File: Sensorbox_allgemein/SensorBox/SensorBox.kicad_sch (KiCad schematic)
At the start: 29 parts, among them J1 SD_Card, Q1 NPN, U2 PS1-O3-100, U3 Beetle ESP32-C6, U5 HPP845E131R5, U6 TPS629211QDRLRQ1

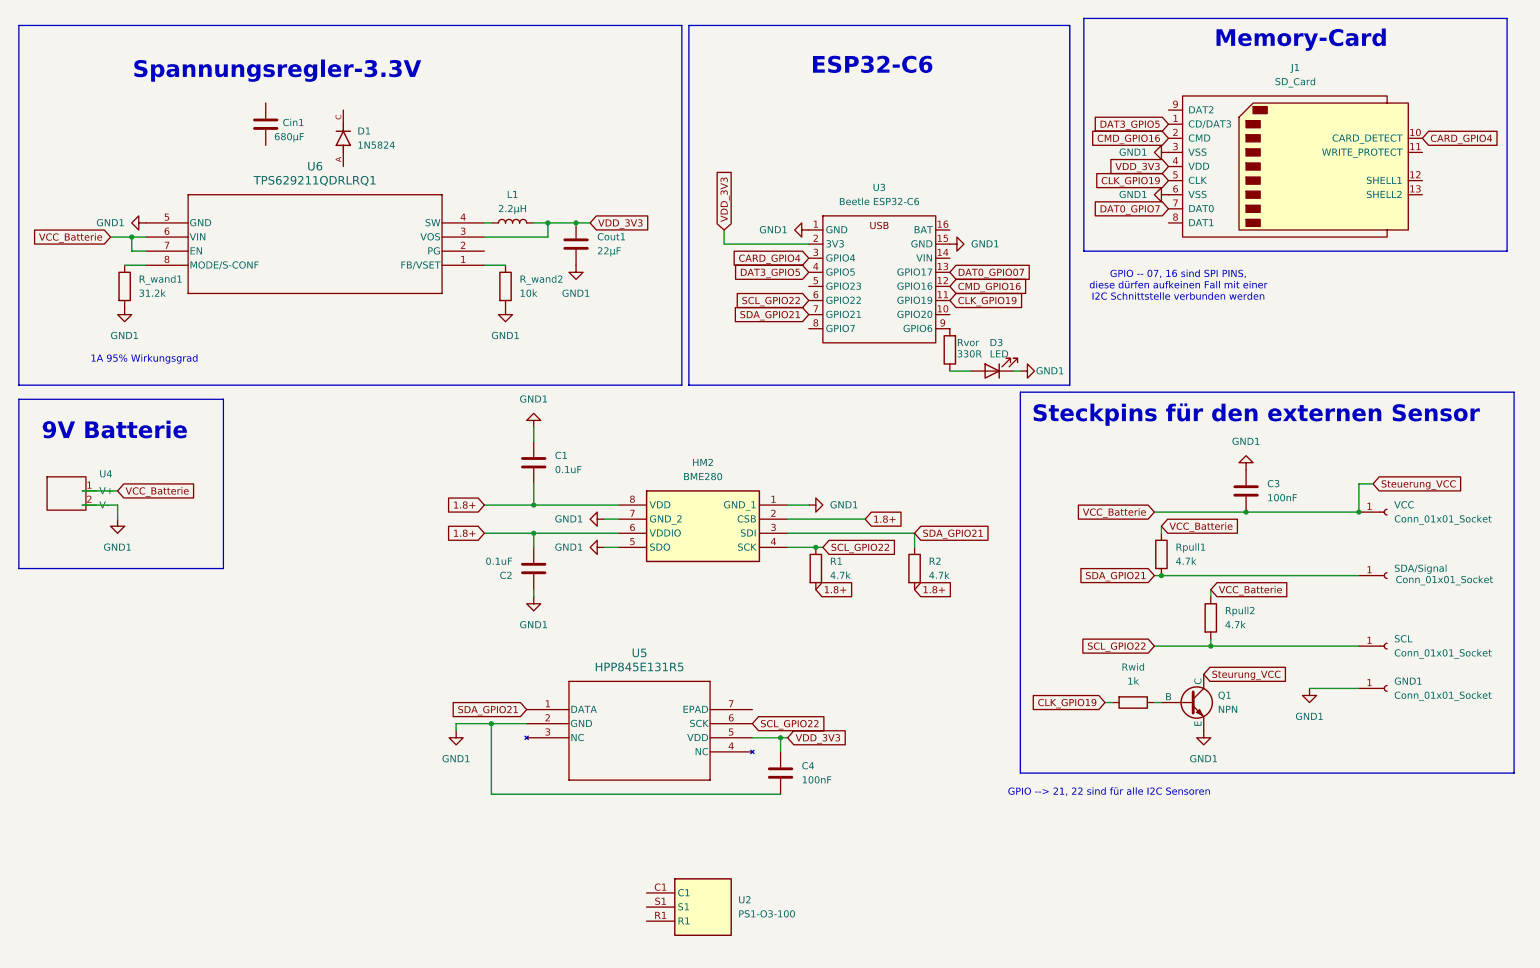
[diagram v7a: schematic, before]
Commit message: Update SensorBox.kicad_sch
pin Belegungen geändert, bzw. angepasst zum Messaufbau. Speziell GPIO20, 19
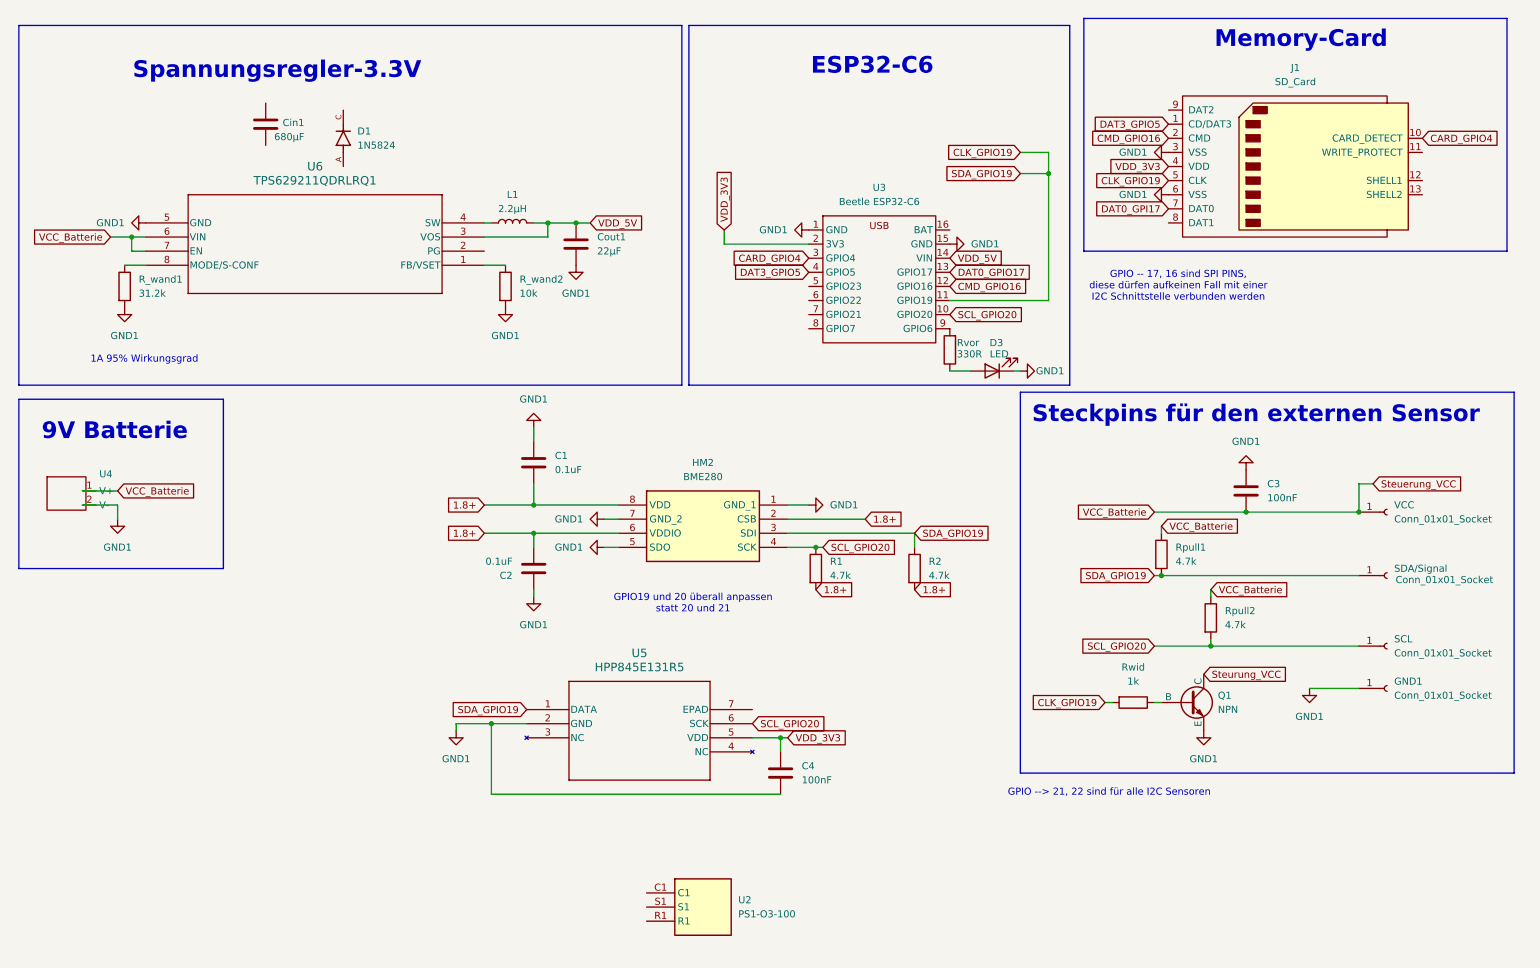
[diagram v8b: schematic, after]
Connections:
- net CLK_GPIO19: now also HM2.3 (SDI), R2.1, Rpull1.2, SDA/Signal.1 (Pin_1), U5.1 (DATA)
- net VDD_3V3: no longer Cout1.1, L1.2, U6.3 (VOS)
- net SCL_GPIO20: now reaches U3.10 (GPIO20)
- net SCL_GPIO20: now also HM2.4 (SCK), R1.1, Rpull2.2, SCL.1 (Pin_1), U5.6 (SCK)
- net VDD_5V: now reaches U3.14 (VIN)
- net VDD_5V: now also Cout1.1, L1.2, U6.3 (VOS)
- net DAT0_GPIO07 renamed DAT0_GPIO17
- net DAT0_GPIO7 renamed DAT0_GPI17
- removed net SCL_GPIO22: HM2.4 (SCK), R1.1, Rpull2.2, SCL.1 (Pin_1), U3.6 (GPIO22), U5.6 (SCK)
- removed net SDA_GPIO21: HM2.3 (SDI), R2.1, Rpull1.2, SDA/Signal.1 (Pin_1), U3.7 (GPIO21), U5.1 (DATA)
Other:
- note added: "GPIO -- 17, 16 sind SPI PINS, diese dürfen aufkeinen Fall mit einer I2C Schnittstelle verbunden werden"
- note added: "GPIO19 und 20 überall anpassen statt 20 und 21"
- note removed: "GPIO -- 07, 16 sind SPI PINS, diese dürfen aufkeinen Fall mit einer I2C Schnittstelle verbunden werden"
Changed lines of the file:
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@@
+	)
+	(junction
+		(at 199.39 41.91)
+		(diameter 0)
+		(color 0 0 0 0)
 	)
 	(junction
@@
 	(wire
 		(pts
+			(xy 194.31 38.1) (xy 199.39 38.1)
+		)
+		(stroke
+			(width 0)
+			(type default)
+		)
+	)
+	(wire
+		(pts
 			(xy 99.06 153.67) (xy 99.06 140.97)
 		)
@@
 	(wire
 		(pts
+			(xy 199.39 64.77) (xy 181.61 64.77)
+		)
+		(stroke
+			(width 0)
+			(type default)
+		)
+	)
+	(wire
+		(pts
 			(xy 31.75 104.14) (xy 31.75 101.6)
 		)
@@
 	(wire
 		(pts
+			(xy 199.39 38.1) (xy 199.39 41.91)
+		)
+		(stroke
+			(width 0)
+			(type default)
+		)
+	)
+	(wire
+		(pts
 			(xy 101.6 58.42) (xy 97.79 58.42)
 		)
@@
 	(wire
 		(pts
+			(xy 194.31 41.91) (xy 199.39 41.91)
+		)
+		(stroke
+			(width 0)
+			(type default)
+		)
+	)
+	(wire
+		(pts
 			(xy 234.95 102.87) (xy 255.27 102.87)
 		)
@@
 		(pts
 			(xy 228.6 127) (xy 255.27 127)
+		)
+		(stroke
+			(width 0)
+			(type default)
+		)
+	)
+	(wire
+		(pts
+			(xy 199.39 41.91) (xy 199.39 64.77)
 		)
 		(stroke
@@
 		)
 	)
-	(text "GPIO -- 07, 16 sind SPI PINS, \ndiese dürfen aufkeinen Fall mit einer \nI2C Schnittstelle verbunden werden"
+	(text "GPIO19 und 20 überall anpassen\nstatt 20 und 21\n"
+		(exclude_from_sim no)
+		(at 135.382 119.38 0)
+		(effects
+			(font
+				(size 1.27 1.27)
+			)
+		)
+	)
+	(text "GPIO -- 17, 16 sind SPI PINS, \ndiese dürfen aufkeinen Fall mit einer \nI2C Schnittstelle verbunden werden"
 		(exclude_from_sim no)
 		(at 222.758 62.23 0)
@@
 		)
 	)
-	(global_label "SCL_GPIO22"
+	(global_label "SCL_GPIO20"
 		(shape input)
 		(at 146.05 140.97 0)
@@
 	(global_label "CLK_GPIO19"
 		(shape input)
-		(at 181.61 64.77 0)
-		(fields_autoplaced yes)
-		(effects
-			(font
-				(size 1.27 1.27)
-			)
-			(justify left)
-		)
-		(property "Intersheetrefs" "${INTERSHEET_REFS}"
-			(at 196.0252 64.77 0)
-			(effects
-				(font
-					(size 1.27 1.27)
-				)
-				(justify left)
-				(hide yes)
-			)
-		)
-	)
-	(global_label "SDA_GPIO21"
+		(at 194.31 38.1 180)
+		(fields_autoplaced yes)
+		(effects
+			(font
+				(size 1.27 1.27)
+			)
+			(justify right)
+		)
+		(property "Intersheetrefs" "${INTERSHEET_REFS}"
+			(at 179.8948 38.1 0)
+			(effects
+				(font
+					(size 1.27 1.27)
+				)
+				(justify right)
+				(hide yes)
+			)
+		)
+	)
+	(global_label "SDA_GPIO19"
 		(shape input)
 		(at 105.41 138.43 180)
@@
 		)
 	)
-	(global_label "SCL_GPIO22"
+	(global_label "SCL_GPIO20"
 		(shape input)
 		(at 158.75 109.22 0)
@@
 		)
 	)
-	(global_label "SDA_GPIO21"
+	(global_label "SDA_GPIO19"
 		(shape input)
 		(at 175.26 106.68 0)
@@
 		)
 	)
+	(global_label "SCL_GPIO20"
+		(shape input)
+		(at 181.61 67.31 0)
+		(fields_autoplaced yes)
+		(effects
+			(font
+				(size 1.27 1.27)
+			)
+			(justify left)
+		)
+		(property "Intersheetrefs" "${INTERSHEET_REFS}"
+			(at 195.9647 67.31 0)
+			(effects
+				(font
+					(size 1.27 1.27)
+				)
+				(justify left)
+				(hide yes)
+			)
+		)
+	)
 	(global_label "1.8+"
 		(shape input)
@@
 		)
 	)
+	(global_label "VDD_5V"
+		(shape input)
+		(at 181.61 57.15 0)
+		(fields_autoplaced yes)
+		(effects
+			(font
+				(size 1.27 1.27)
+			)
+			(justify left)
+		)
+		(property "Intersheetrefs" "${INTERSHEET_REFS}"
+			(at 191.4895 57.15 0)
+			(effects
+				(font
+					(size 1.27 1.27)
+				)
+				(justify left)
+				(hide yes)
+			)
+		)
+	)
 	(global_label "1.8+"
 		(shape input)
@@
 		)
 	)
-	(global_label "DAT0_GPIO07"
+	(global_label "DAT0_GPIO17"
 		(shape input)
 		(at 181.61 59.69 0)
@@
 		)
 	)
-	(global_label "SCL_GPIO22"
+	(global_label "SCL_GPIO20"
 		(shape input)
 		(at 218.44 127 180)
@@
 		)
 	)
-	(global_label "SCL_GPIO22"
-		(shape input)
-		(at 156.21 64.77 180)
-		(fields_autoplaced yes)
-		(effects
-			(font
-				(size 1.27 1.27)
-			)
-			(justify right)
-		)
-		(property "Intersheetrefs" "${INTERSHEET_REFS}"
-			(at 141.8553 64.77 0)
-			(effects
-				(font
-					(size 1.27 1.27)
-				)
-				(justify right)
-				(hide yes)
-			)
-		)
-	)
-	(global_label "SDA_GPIO21"
+	(global_label "SDA_GPIO19"
 		(shape input)
 		(at 218.44 114.3 180)
@@
 		)
 	)
-	(global_label "SDA_GPIO21"
-		(shape input)
-		(at 156.21 67.31 180)
-		(fields_autoplaced yes)
-		(effects
-			(font
-				(size 1.27 1.27)
-			)
-			(justify right)
-		)
-		(property "Intersheetrefs" "${INTERSHEET_REFS}"
-			(at 141.7948 67.31 0)
-			(effects
-				(font
-					(size 1.27 1.27)
-				)
-				(justify right)
-				(hide yes)
-			)
-		)
-	)
 	(global_label "CARD_GPIO4"
 		(shape input)
@@
 		)
 	)
-	(global_label "DAT0_GPIO7"
+	(global_label "DAT0_GPI17"
 		(shape input)
 		(at 220.98 48.26 180)
@@
 		)
 		(property "Intersheetrefs" "${INTERSHEET_REFS}"
-			(at 206.8067 48.26 0)
+			(at 206.9277 48.26 0)
+			(effects
+				(font
+					(size 1.27 1.27)
+				)
+				(justify right)
+				(hide yes)
+			)
+		)
+	)
+	(global_label "SDA_GPIO19"
+		(shape input)
+		(at 194.31 41.91 180)
+		(fields_autoplaced yes)
+		(effects
+			(font
+				(size 1.27 1.27)
+			)
+			(justify right)
+		)
+		(property "Intersheetrefs" "${INTERSHEET_REFS}"
+			(at 179.8948 41.91 0)
 			(effects
 				(font
@@
 		)
 	)
-	(global_label "VDD_3V3"
+	(global_label "VDD_5V"
 		(shape input)
 		(at 116.84 50.8 0)
@@
 		)
 		(property "Intersheetrefs" "${INTERSHEET_REFS}"
-			(at 127.929 50.8 0)
-			(effects
-				(font
+			(at 126.7195 50.8 0)
+			(effects
+				(font
